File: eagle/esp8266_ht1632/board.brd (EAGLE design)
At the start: 42.2 x 26 mm, 11 parts, among them IC1 LM1117MP-3.3

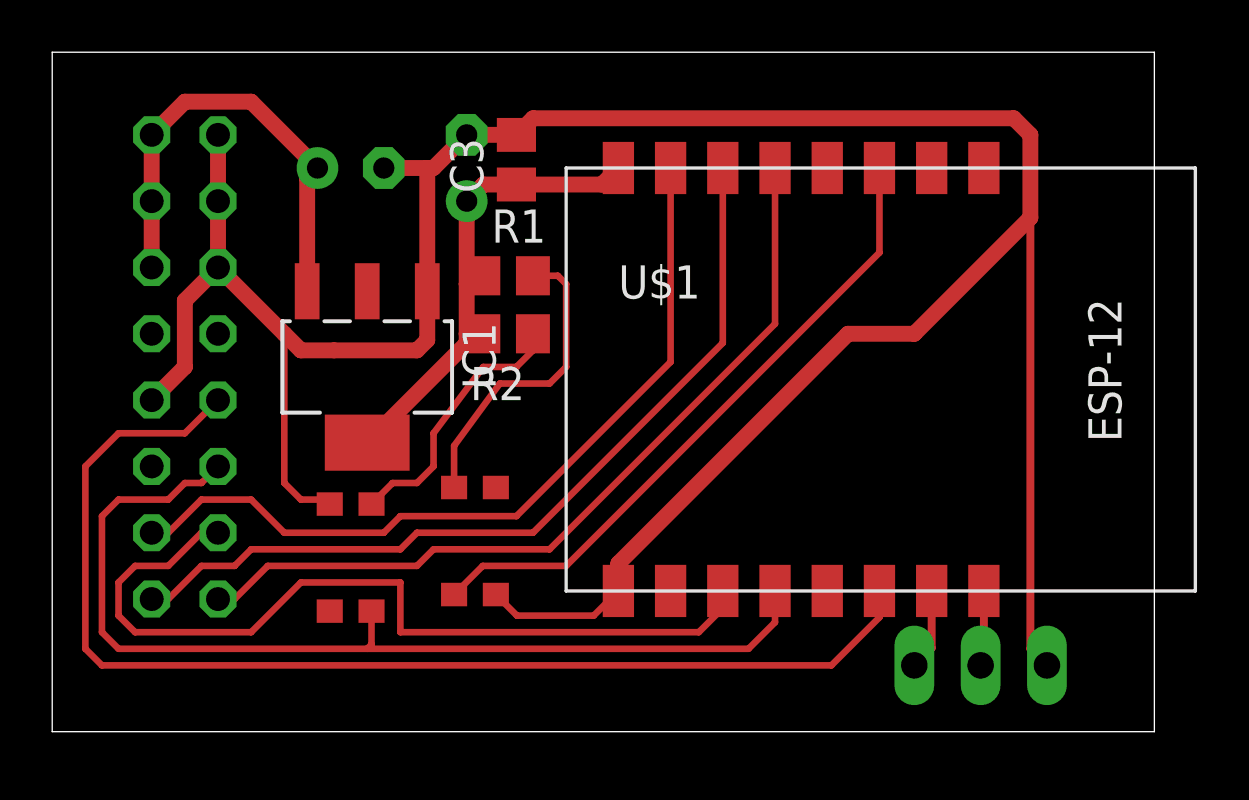
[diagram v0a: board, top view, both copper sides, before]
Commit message: resize board; add gitignore for eagle
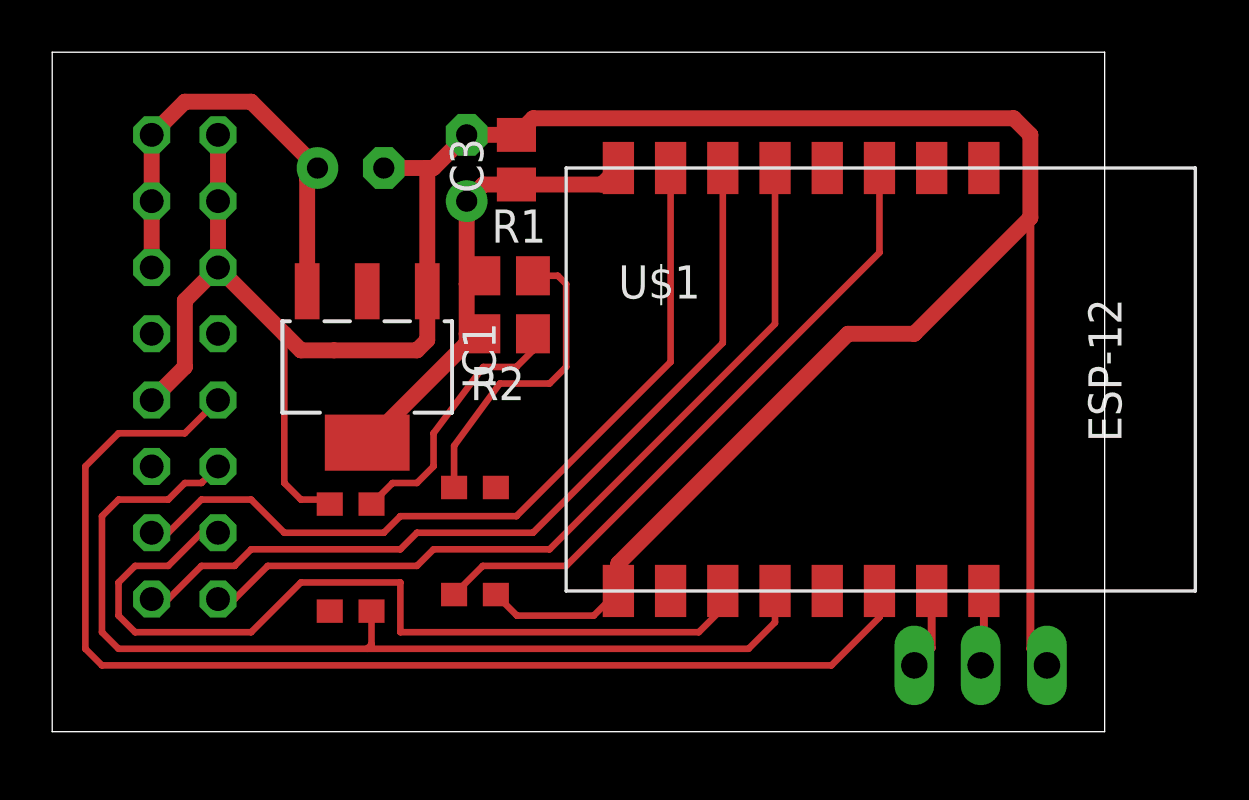
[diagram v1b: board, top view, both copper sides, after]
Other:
- board size 42.2 x 26 mm -> 40.3 x 26 mm
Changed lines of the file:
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@@
 <board>
 <plain>
-<wire x1="0" y1="0" x2="42.215" y2="0" width="0" layer="20"/>
-<wire x1="42.215" y1="0" x2="42.215" y2="26.025" width="0" layer="20"/>
-<wire x1="42.215" y1="26.025" x2="0" y2="26.025" width="0" layer="20"/>
+<wire x1="0" y1="0" x2="40.31" y2="0" width="0" layer="20"/>
+<wire x1="40.31" y1="0" x2="40.31" y2="26.025" width="0" layer="20"/>
+<wire x1="40.31" y1="26.025" x2="0" y2="26.025" width="0" layer="20"/>
 <wire x1="0" y1="26.025" x2="0" y2="0" width="0" layer="20"/>
 </plain>

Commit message: board optimization; fix esp pinout
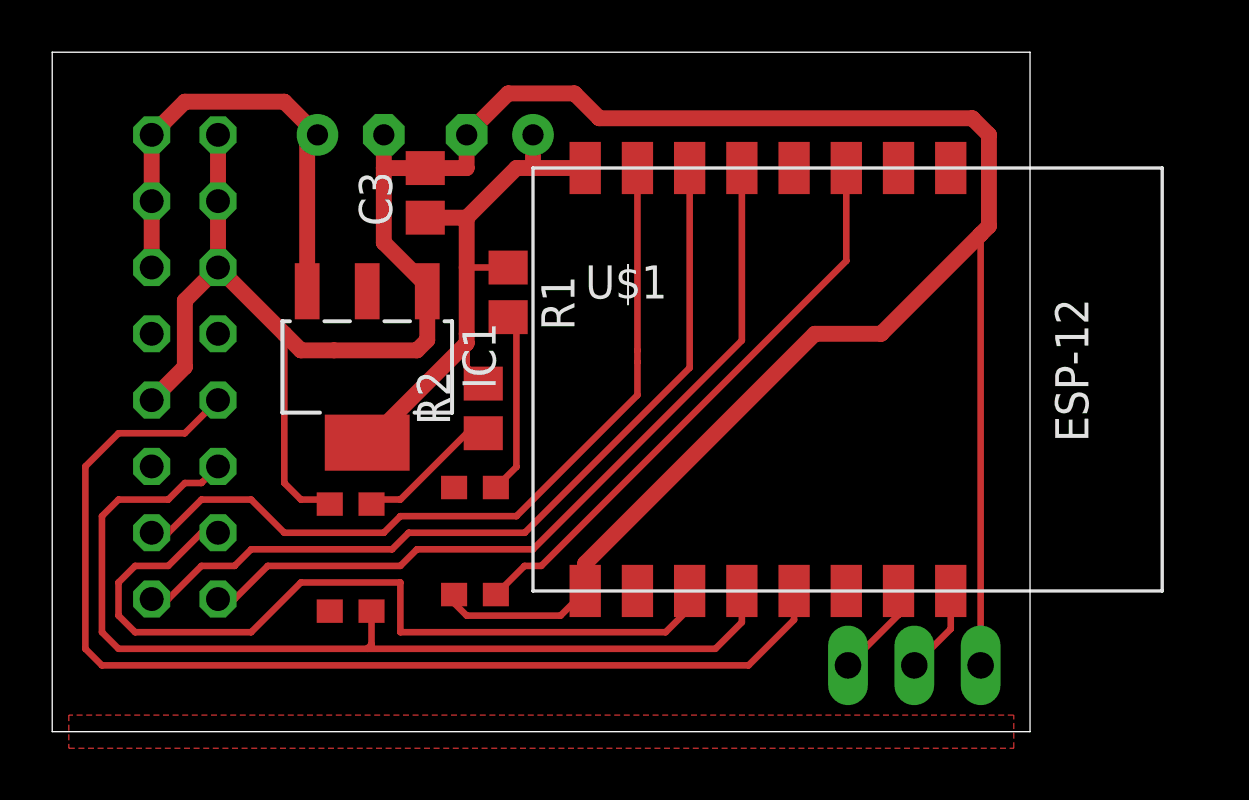
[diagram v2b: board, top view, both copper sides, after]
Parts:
- moved C3 3.72 mm to (14.3, 20.6)
- moved R2 3.01 mm to (16.5, 12.4), turned to 90 degrees
- moved SV2 2.54 mm to (33.0, 2.54)
- moved C2 1.80 mm to (17.1, 22.9), turned to 0 degrees
- moved C1 1.27 mm to (11.4, 22.9)
- moved U$1 1.27 mm to (18.4, 21.6)
- moved R1 0.63 mm to (17.5, 16.8), turned to 270 degrees
- turned U$2 to 90 degrees
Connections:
- net DATA: now also U$1.5; no longer U$1.6
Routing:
- net N$1: track 36.9 -> 29.3 mm
- net WR: track 49.3 -> 43.0 mm
- net +3V3: track 18.6 -> 22.1 mm
- net DATA: track 45.6 -> 42.4 mm
- net GND: track 109.5 -> 110.9 mm
- net CS1: track 33.0 -> 31.7 mm
- net CS2: track 31.7 -> 30.8 mm
- net +5V: track 17.9 -> 18.8 mm
- net CS3: track 32.6 -> 31.9 mm
- net CS4: track 31.1 -> 30.5 mm
- net RXD: track 3.13 -> 3.65 mm
- net TXD: track 2.90 -> 3.43 mm
- added copper zone on layer 1, net GND
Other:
- board size 40.3 x 26 mm -> 37.5 x 26 mm
